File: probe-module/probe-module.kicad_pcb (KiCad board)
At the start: 2 copper layers, 1 part

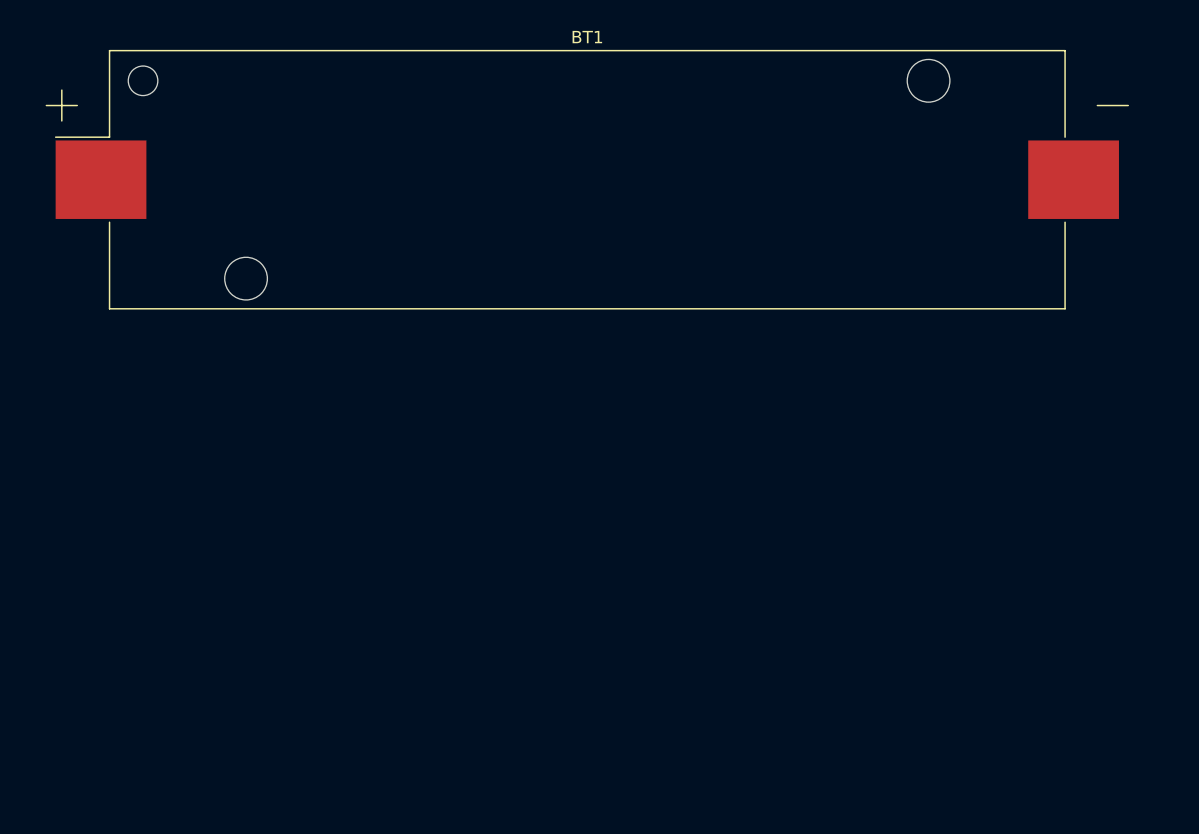
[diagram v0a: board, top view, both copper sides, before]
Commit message: Fix too low net clearance
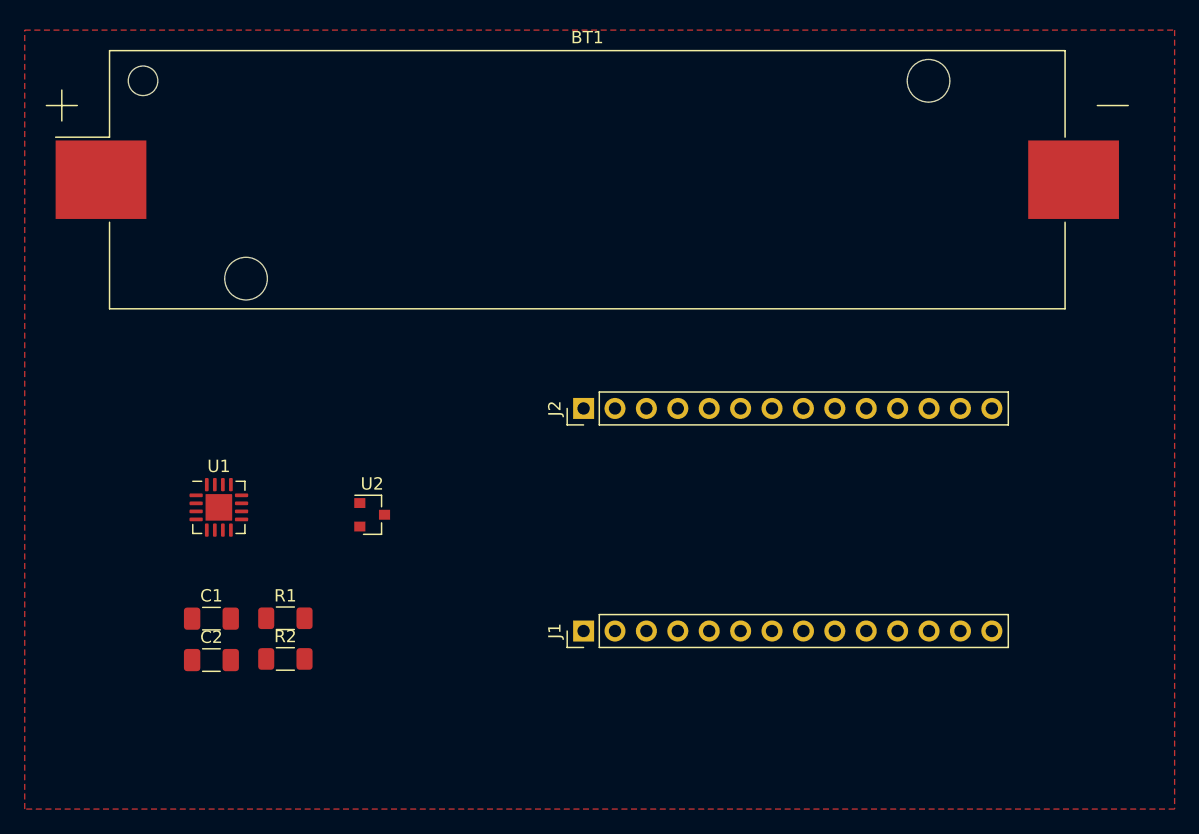
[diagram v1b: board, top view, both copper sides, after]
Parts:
- added C1: 100nF, Capacitor_SMD:C_1206_3216Metric_Pad1.33x1.80mm_HandSolder, F.Cu at (119.1, 106.6)
- added C2: 100uF, Capacitor_SMD:C_1206_3216Metric_Pad1.33x1.80mm_HandSolder, F.Cu at (119.1, 110.0)
- added J1: Conn_01x14, Connector_PinHeader_2.54mm:PinHeader_1x14_P2.54mm_Vertical, F.Cu at (149.2, 107.6)
- added J2: Conn_01x14, Connector_PinHeader_2.54mm:PinHeader_1x14_P2.54mm_Vertical, F.Cu at (149.2, 89.6)
- added R1: 27k, Resistor_SMD:R_1206_3216Metric_Pad1.30x1.75mm_HandSolder, F.Cu at (125.1, 106.6)
- added R2: 100k, Resistor_SMD:R_1206_3216Metric_Pad1.30x1.75mm_HandSolder, F.Cu at (125.1, 109.9)
- added U1: LTC4055, Package_DFN_QFN:QFN-16-1EP_4x4mm_P0.65mm_EP2.15x2.15mm, F.Cu at (119.7, 97.6)
- added U2: MCP1700-3302E_SOT23, Package_TO_SOT_SMD:SOT-23, F.Cu at (132.1, 98.2)
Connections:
- BT1 pad 1: +BATT -> (no net)
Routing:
- added copper zone on F.Cu, net GND
